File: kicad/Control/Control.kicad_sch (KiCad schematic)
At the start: 27 parts, among them J1 Conn_01x20_Pin, J2 Conn_01x05_Pin, J3 Screw_Terminal_01x02, J4 Conn_02x05_Odd_Even, J5 Conn_02x05_Odd_Even, SW1 PRESET1, SW2 CH2_EN, SW3 PRESET2, SW4 COARSE, SW5 CH1_EN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

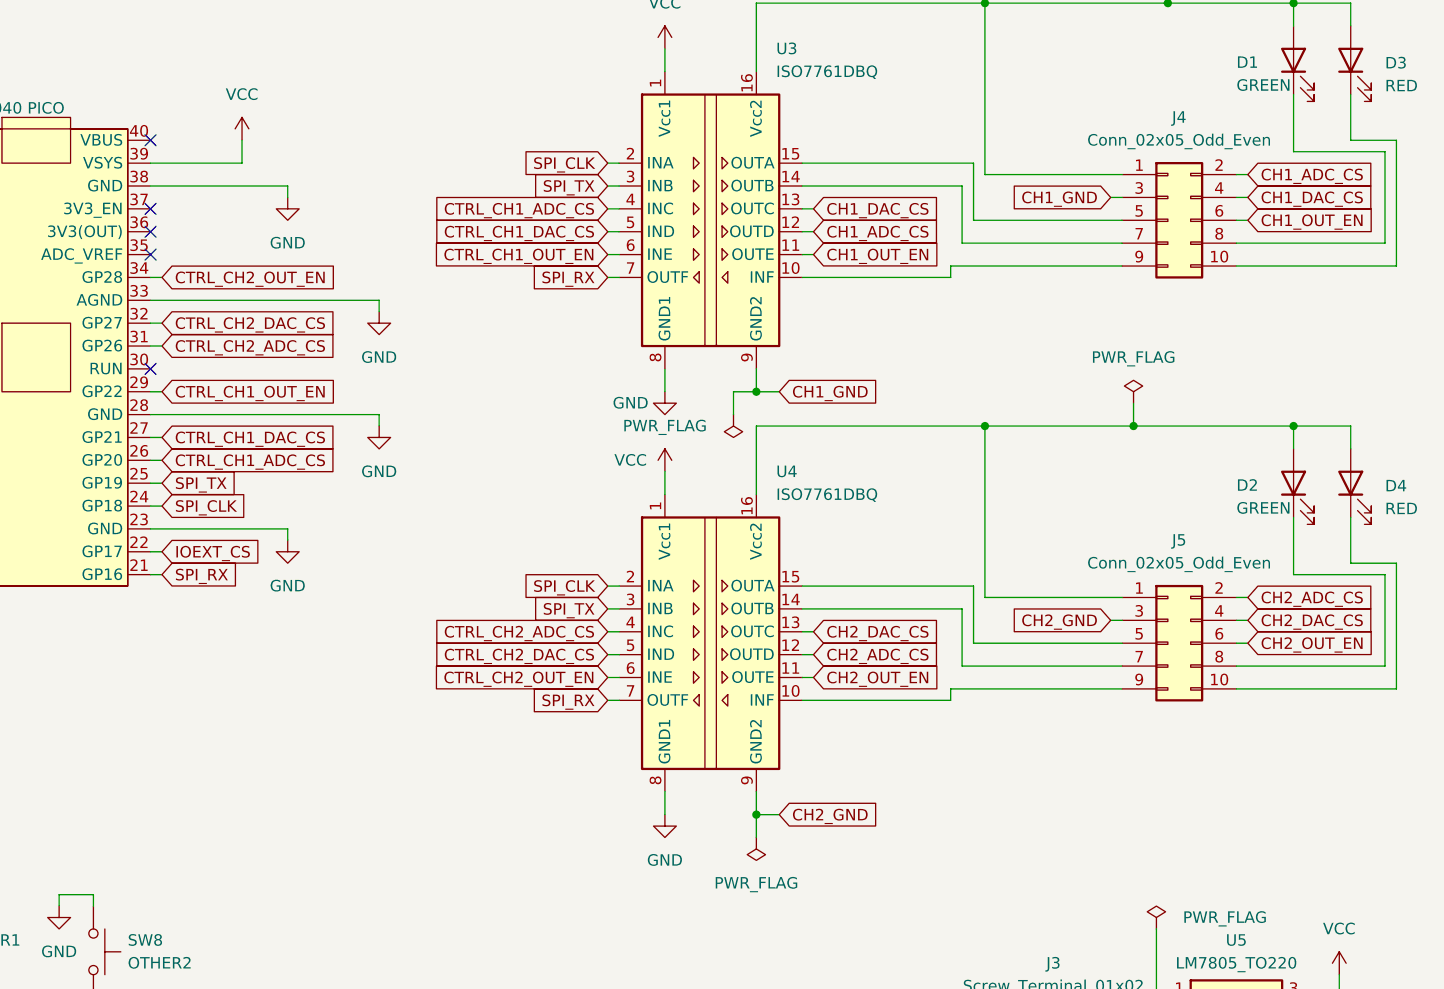
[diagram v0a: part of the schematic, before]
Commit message: Fix control connectors spacing
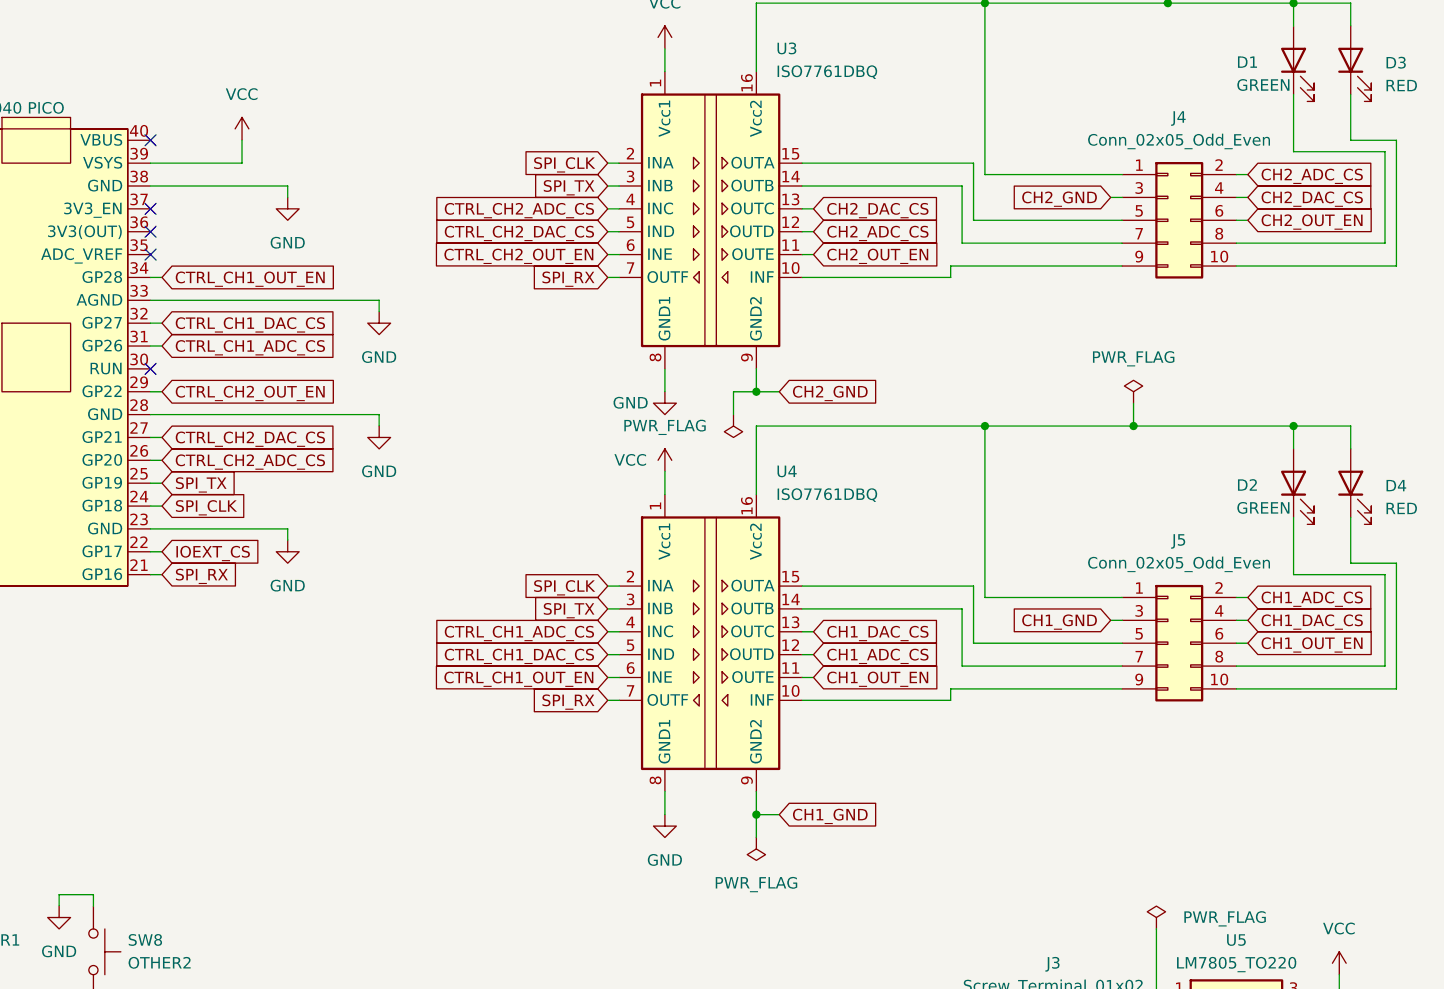
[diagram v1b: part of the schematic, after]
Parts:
- J4, J5: footprint Connector_PinHeader_2.54mm:PinHeader_2x05_P2.54mm_Vertical -> Altbutt:Connector Header 2x05
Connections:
- net CH1_ADC_CS: now also J5.2 (Pin_2), U4.12 (OUTD); no longer J4.2 (Pin_2), U3.12 (OUTD)
- net CH1_DAC_CS: now also J5.4 (Pin_4), U4.13 (OUTC); no longer J4.4 (Pin_4), U3.13 (OUTC)
- net CH1_GND: now also J5.3 (Pin_3), U4.9 (GND2); no longer J4.3 (Pin_3), U3.9 (GND2)
- net CH1_OUT_EN: now also J5.6 (Pin_6), U4.11 (OUTE); no longer J4.6 (Pin_6), U3.11 (OUTE)
- net CH2_ADC_CS: now also J4.2 (Pin_2), U3.12 (OUTD); no longer J5.2 (Pin_2), U4.12 (OUTD)
- net CH2_DAC_CS: now also J4.4 (Pin_4), U3.13 (OUTC); no longer J5.4 (Pin_4), U4.13 (OUTC)
- net CH2_GND: now also J4.3 (Pin_3), U3.9 (GND2); no longer J5.3 (Pin_3), U4.9 (GND2)
- net CH2_OUT_EN: now also J4.6 (Pin_6), U3.11 (OUTE); no longer J5.6 (Pin_6), U4.11 (OUTE)
- net CTRL_CH1_ADC_CS: now also U2.31 (GP26), U4.4 (INC); no longer U2.26 (GP20), U3.4 (INC)
- net CTRL_CH1_DAC_CS: now also U2.32 (GP27), U4.5 (IND); no longer U2.27 (GP21), U3.5 (IND)
- net CTRL_CH1_OUT_EN: now also U2.34 (GP28), U4.6 (INE); no longer U2.29 (GP22), U3.6 (INE)
- net CTRL_CH2_ADC_CS: now also U2.26 (GP20), U3.4 (INC); no longer U2.31 (GP26), U4.4 (INC)
- net CTRL_CH2_DAC_CS: now also U2.27 (GP21), U3.5 (IND); no longer U2.32 (GP27), U4.5 (IND)
- net CTRL_CH2_OUT_EN: now also U2.29 (GP22), U3.6 (INE); no longer U2.34 (GP28), U4.6 (INE)
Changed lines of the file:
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@@
 		)
 	)
-	(global_label "CTRL_CH1_ADC_CS"
+	(global_label "CTRL_CH2_ADC_CS"
 		(shape input)
 		(at 139.7 67.31 0)
@@
 		)
 	)
-	(global_label "CH1_GND"
+	(global_label "CH2_GND"
 		(shape input)
 		(at 208.28 59.69 0)
@@
 		)
 	)
-	(global_label "CH2_GND"
+	(global_label "CH1_GND"
 		(shape input)
 		(at 245.11 85.09 180)
@@
 		)
 	)
-	(global_label "CH2_DAC_CS"
+	(global_label "CH1_DAC_CS"
 		(shape input)
 		(at 260.35 85.09 0)
@@
 		)
 	)
-	(global_label "CH2_OUT_EN"
+	(global_label "CH1_OUT_EN"
 		(shape input)
 		(at 212.09 91.44 0)
@@
 		)
 	)
-	(global_label "CH2_ADC_CS"
+	(global_label "CH1_ADC_CS"
 		(shape input)
 		(at 212.09 88.9 0)
@@
 		)
 	)
-	(global_label "CH2_OUT_EN"
+	(global_label "CH1_OUT_EN"
 		(shape input)
 		(at 260.35 87.63 0)
@@
 		)
 	)
-	(global_label "CTRL_CH2_OUT_EN"
+	(global_label "CTRL_CH1_OUT_EN"
 		(shape input)
 		(at 189.23 91.44 180)
@@
 		)
 	)
-	(global_label "CH1_DAC_CS"
+	(global_label "CH2_DAC_CS"
 		(shape input)
 		(at 212.09 39.37 0)
@@
 		)
 	)
-	(global_label "CTRL_CH2_DAC_CS"
+	(global_label "CTRL_CH1_DAC_CS"
 		(shape input)
 		(at 189.23 88.9 180)
@@
 		)
 	)
-	(global_label "CTRL_CH2_OUT_EN"
+	(global_label "CTRL_CH1_OUT_EN"
 		(shape input)
 		(at 139.7 46.99 0)
@@
 		)
 	)
-	(global_label "CTRL_CH1_ADC_CS"
+	(global_label "CTRL_CH2_ADC_CS"
 		(shape input)
 		(at 189.23 39.37 180)
@@
 		)
 	)
-	(global_label "CH1_DAC_CS"
+	(global_label "CH2_DAC_CS"
 		(shape input)
 		(at 260.35 38.1 0)
@@
 		)
 	)
-	(global_label "CH1_ADC_CS"
+	(global_label "CH2_ADC_CS"
 		(shape input)
 		(at 212.09 41.91 0)
@@
 		)
 	)
-	(global_label "CTRL_CH1_DAC_CS"
+	(global_label "CTRL_CH2_DAC_CS"
 		(shape input)
 		(at 189.23 41.91 180)
@@
 		)
 	)
-	(global_label "CH1_ADC_CS"
+	(global_label "CH2_ADC_CS"
 		(shape input)
 		(at 260.35 35.56 0)
@@
 		)
 	)
-	(global_label "CTRL_CH1_OUT_EN"
+	(global_label "CTRL_CH2_OUT_EN"
 		(shape input)
 		(at 139.7 59.69 0)
@@
 		)
 	)
-	(global_label "CH2_DAC_CS"
+	(global_label "CH1_DAC_CS"
 		(shape input)
 		(at 212.09 86.36 0)
@@
 		)
 	)
-	(global_label "CTRL_CH2_DAC_CS"
+	(global_label "CTRL_CH1_DAC_CS"
 		(shape input)
 		(at 139.7 52.07 0)
@@
 		)
 	)
-	(global_label "CH2_ADC_CS"
+	(global_label "CH1_ADC_CS"
 		(shape input)
 		(at 260.35 82.55 0)
@@
 		)
 	)
-	(global_label "CH1_OUT_EN"
+	(global_label "CH2_OUT_EN"
 		(shape input)
 		(at 212.09 44.45 0)
@@
 		)
 	)
-	(global_label "CTRL_CH2_ADC_CS"
+	(global_label "CTRL_CH1_ADC_CS"
 		(shape input)
 		(at 139.7 54.61 0)
@@
 		)
 	)
-	(global_label "CH2_GND"
+	(global_label "CH1_GND"
 		(shape input)
 		(at 208.28 106.68 0)
@@
 		)
 	)
-	(global_label "CTRL_CH1_DAC_CS"
+	(global_label "CTRL_CH2_DAC_CS"
 		(shape input)
 		(at 139.7 64.77 0)
@@
 		)
 	)
-	(global_label "CTRL_CH2_ADC_CS"
+	(global_label "CTRL_CH1_ADC_CS"
 		(shape input)
 		(at 189.23 86.36 180)
@@
 		)
 	)
-	(global_label "CTRL_CH1_OUT_EN"
+	(global_label "CTRL_CH2_OUT_EN"
 		(shape input)
 		(at 189.23 44.45 180)
@@
 		)
 	)
-	(global_label "CH1_GND"
+	(global_label "CH2_GND"
 		(shape input)
 		(at 245.11 38.1 180)
@@
 		)
 	)
-	(global_label "CH1_OUT_EN"
+	(global_label "CH2_OUT_EN"
 		(shape input)
 		(at 260.35 40.64 0)
@@
 			)
 		)
-		(property "Footprint" "Connector_PinHeader_2.54mm:PinHeader_2x05_P2.54mm_Vertical"
+		(property "Footprint" "Altbutt:Connector Header 2x05"
 			(at 251.46 87.63 0)
 			(effects
@@
 			)
 		)
-		(property "Footprint" "Connector_PinHeader_2.54mm:PinHeader_2x05_P2.54mm_Vertical"
+		(property "Footprint" "Altbutt:Connector Header 2x05"
 			(at 251.46 40.64 0)
 			(effects
